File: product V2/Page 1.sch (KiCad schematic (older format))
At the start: 35 parts, among them J1 10118192-0001LF, J2 ARJM11A3, J3 Conn_02x05_Odd_Even, U1 AZ1117-3.3, U2 LAN8720A

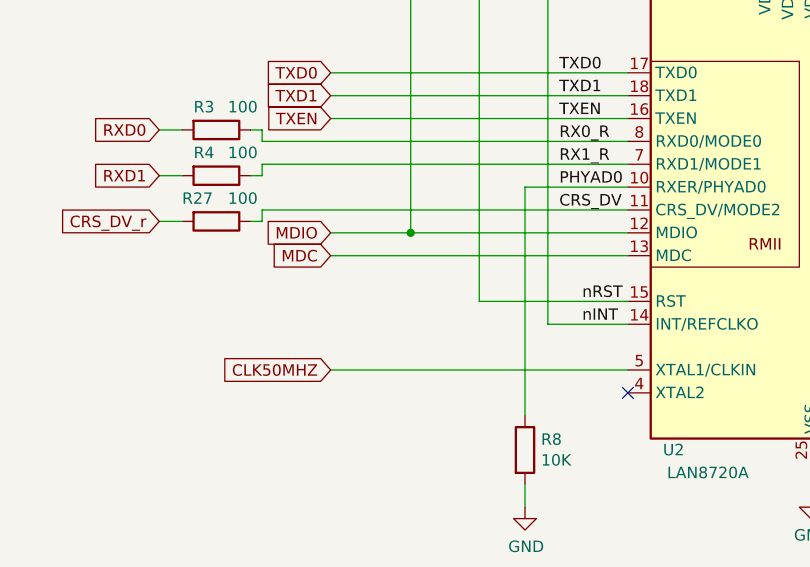
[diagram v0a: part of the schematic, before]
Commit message: Editted traces to improve signal intregrity
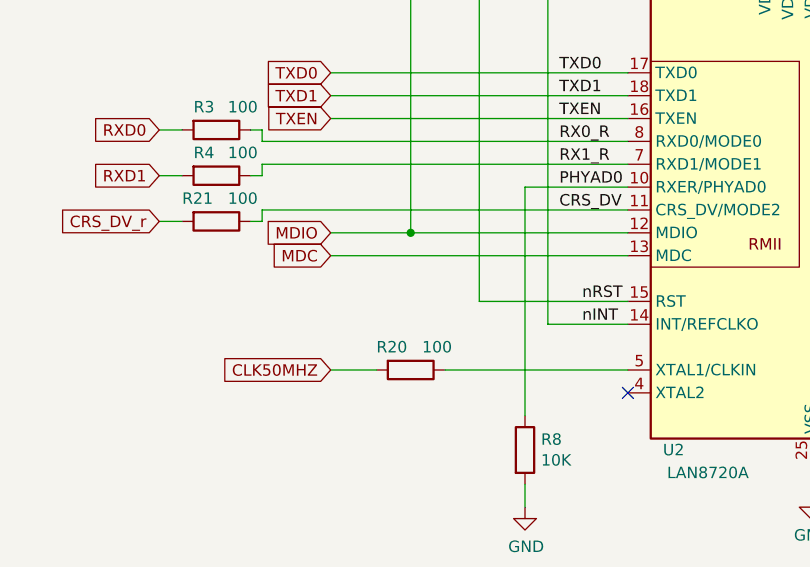
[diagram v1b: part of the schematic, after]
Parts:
- added R20: 100, Resistor_SMD:R_0603_1608Metric, symbol Device:R
- renumbered R27 to R21
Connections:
- net CLK50MHZ: now also R20.2; no longer U2.5 (XTAL1/CLKIN)
- new net: R20.1, U2.5 (XTAL1/CLKIN)
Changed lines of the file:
@@
 EESchema Schematic File Version 4
+LIBS:EsperDNS-cache
 EELAYER 30 0
 EELAYER END
@@
 Wire Wire Line
 	3850 4800 2550 4800
-Wire Wire Line
-	3850 5300 2550 5300
 Connection ~ 7150 4500
 Wire Wire Line
@@
 P 2050 4650
 AR Path="/5DFF908E" Ref="R?"  Part="1"
-AR Path="/5DED2F9B/5DFF908E" Ref="R27"  Part="1"
-F 0 "R27" V 1950 4500 50  0000 L CNN
+AR Path="/5DED2F9B/5DFF908E" Ref="R21"  Part="1"
+F 0 "R21" V 1950 4500 50  0000 L CNN
 F 1 "100" V 1950 4700 50  0000 L CNN
 F 2 "Resistor_SMD:R_0603_1608Metric" V 1980 4650 50  0001 C CNN
@@
 	-1   0    0    -1
 $EndComp
+$Comp
+L Device:R R?
+U 1 1 5F488106
+P 2900 5300
+AR Path="/5F488106" Ref="R?"  Part="1"
+AR Path="/5DED2F9B/5F488106" Ref="R20"  Part="1"
+F 0 "R20" V 2800 5150 50  0000 L CNN
+F 1 "100" V 2800 5350 50  0000 L CNN
+F 2 "Resistor_SMD:R_0603_1608Metric" V 2830 5300 50  0001 C CNN
+F 3 "~" H 2900 5300 50  0001 C CNN
+F 4 "C105588" H 2900 5300 50  0001 C CNN "LCSC Part Number"
+	1    2900 5300
+	0    1    1    0
+$EndComp
+Wire Wire Line
+	2550 5300 2750 5300
+Wire Wire Line
+	3050 5300 3850 5300
 $EndSCHEMATC

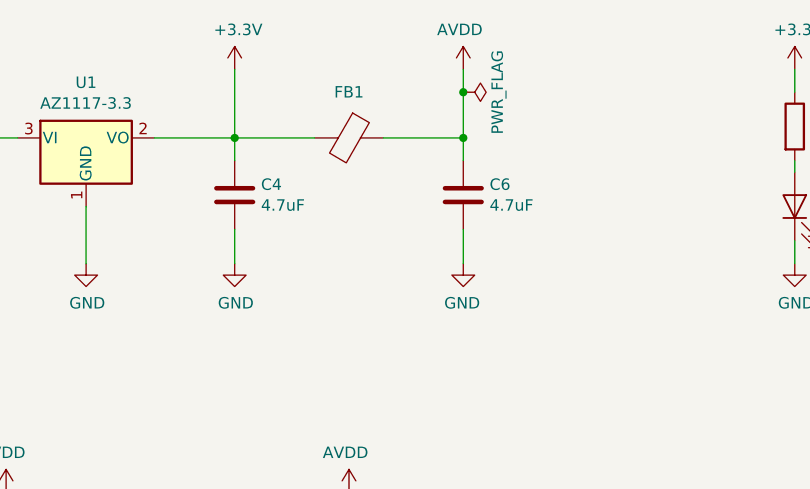
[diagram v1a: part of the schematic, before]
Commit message: Changed board outline and mounting to better fit inside enclosure
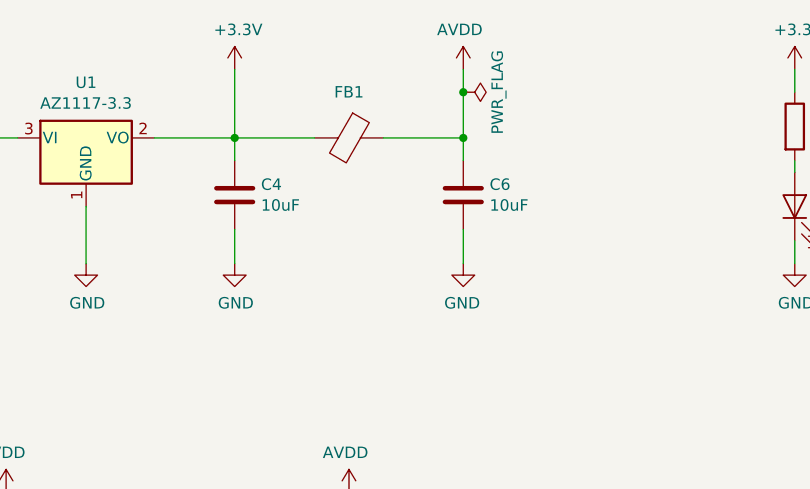
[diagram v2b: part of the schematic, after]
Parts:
- C4, C6: value 4.7uF -> 10uF
- J1: footprint digikey-footprints:USB_Micro_B_Female_10118192 -> My Footprints:USB_Micro_B_Female_10118192
- U2: footprint Package_DFN_QFN:QFN-24-1EP_4x4mm_P0.5mm_EP2.6x2.6mm -> My Footprints:QFN-24-1EP_4x4mm_P0.5mm_EP2.6x2.6mm
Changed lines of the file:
@@
 EESchema Schematic File Version 4
-LIBS:EsperDNS-cache
 EELAYER 30 0
 EELAYER END
@@
 AR Path="/5DED2F9B/5DF04C26" Ref="C4"  Part="1"
 F 0 "C4" H 5865 1846 50  0000 L CNN
-F 1 "4.7uF" H 5865 1755 50  0000 L CNN
+F 1 "10uF" H 5865 1755 50  0000 L CNN
 F 2 "Capacitor_SMD:C_0603_1608Metric" H 5788 1650 50  0001 C CNN
 F 3 "~" H 5750 1800 50  0001 C CNN
@@
 AR Path="/5DED2F9B/5DF04D40" Ref="C6"  Part="1"
 F 0 "C6" H 6635 1846 50  0000 R CNN
-F 1 "4.7uF" H 6635 1755 50  0000 R CNN
+F 1 "10uF" H 6635 1755 50  0000 R CNN
 F 2 "Capacitor_SMD:C_0603_1608Metric" H 6788 1650 50  0001 C CNN
 F 3 "~" H 6750 1800 50  0001 C CNN
@@
 F 0 "J1" H 1807 1975 50  0000 C CNN
 F 1 "10118192-0001LF" H 1807 1976 50  0001 C CNN
-F 2 "digikey-footprints:USB_Micro_B_Female_10118192" H 1900 1550 50  0001 C CNN
+F 2 "My Footprints:USB_Micro_B_Female_10118192" H 1900 1550 50  0001 C CNN
 F 3 "~" H 1900 1550 50  0001 C CNN
 F 4 "C132564" H 1750 1600 50  0001 C CNN "LCSC Part Number"
@@
 F 0 "U2" H 4050 3550 50  0000 C CNN
 F 1 "LAN8720A" H 4200 3450 50  0000 C CNN
-F 2 "Package_DFN_QFN:QFN-24-1EP_4x4mm_P0.5mm_EP2.6x2.6mm" H 4700 3550 50  0001 L CNN
+F 2 "My Footprints:QFN-24-1EP_4x4mm_P0.5mm_EP2.6x2.6mm" H 4700 3550 50  0001 L CNN
 F 3 "http://ww1.microchip.com/downloads/en/DeviceDoc/8720a.pdf" H 4450 3650 50  0001 C CNN
 F 4 "C45223" H 4650 4600 50  0001 C CNN "LCSC Part Number"
@@
 	0    1    1    0
 $EndComp
-$Comp
-L Device:R R?
-U 1 1 5DFE6B8F
-P 2050 4450
-AR Path="/5DFE6B8F" Ref="R?"  Part="1"
-AR Path="/5DED2F9B/5DFE6B8F" Ref="R4"  Part="1"
-F 0 "R4" V 1950 4350 50  0000 L CNN
-F 1 "100" V 1950 4500 50  0000 L CNN
-F 2 "Resistor_SMD:R_0603_1608Metric" V 1980 4450 50  0001 C CNN
-F 3 "~" H 2050 4450 50  0001 C CNN
-F 4 "C105588" H 2050 4450 50  0001 C CNN "LCSC Part Number"
-	1    2050 4450
-	0    1    1    0
-$EndComp
 Wire Wire Line
 	3850 4300 2250 4300
@@
 Wire Wire Line
 	2250 4650 2250 4600
-$Comp
-L Device:R R?
-U 1 1 5DFF908E
-P 2050 4650
-AR Path="/5DFF908E" Ref="R?"  Part="1"
-AR Path="/5DED2F9B/5DFF908E" Ref="R21"  Part="1"
-F 0 "R21" V 1950 4500 50  0000 L CNN
-F 1 "100" V 1950 4700 50  0000 L CNN
-F 2 "Resistor_SMD:R_0603_1608Metric" V 1980 4650 50  0001 C CNN
-F 3 "~" H 2050 4650 50  0001 C CNN
-F 4 "C105588" H 2050 4650 50  0001 C CNN "LCSC Part Number"
-	1    2050 4650
-	0    1    1    0
-$EndComp
 Text Label 3650 5000 0    50   ~ 0
 nRST
@@
 Wire Wire Line
 	3050 5300 3850 5300
+$Comp
+L Device:R R?
+U 1 1 5DFE6B8F
+P 2050 4450
+AR Path="/5DFE6B8F" Ref="R?"  Part="1"
+AR Path="/5DED2F9B/5DFE6B8F" Ref="R4"  Part="1"
+F 0 "R4" V 1950 4350 50  0000 L CNN
+F 1 "100" V 1950 4500 50  0000 L CNN
+F 2 "Resistor_SMD:R_0603_1608Metric" V 1980 4450 50  0001 C CNN
+F 3 "~" H 2050 4450 50  0001 C CNN
+F 4 "C105588" H 2050 4450 50  0001 C CNN "LCSC Part Number"
+	1    2050 4450
+	0    1    1    0
+$EndComp
+$Comp
+L Device:R R?
+U 1 1 5DFF908E
+P 2050 4650
+AR Path="/5DFF908E" Ref="R?"  Part="1"
+AR Path="/5DED2F9B/5DFF908E" Ref="R21"  Part="1"
+F 0 "R21" V 1950 4500 50  0000 L CNN
+F 1 "100" V 1950 4700 50  0000 L CNN
+F 2 "Resistor_SMD:R_0603_1608Metric" V 1980 4650 50  0001 C CNN
+F 3 "~" H 2050 4650 50  0001 C CNN
+F 4 "C105588" H 2050 4650 50  0001 C CNN "LCSC Part Number"
+	1    2050 4650
+	0    1    1    0
+$EndComp
 $EndSCHEMATC
